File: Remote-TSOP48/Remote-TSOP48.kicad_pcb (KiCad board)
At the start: 2 copper layers, 32 x 23 mm, 12 parts, among them J1 FFC-50, J6 SHIELD, U1 TSOP-48

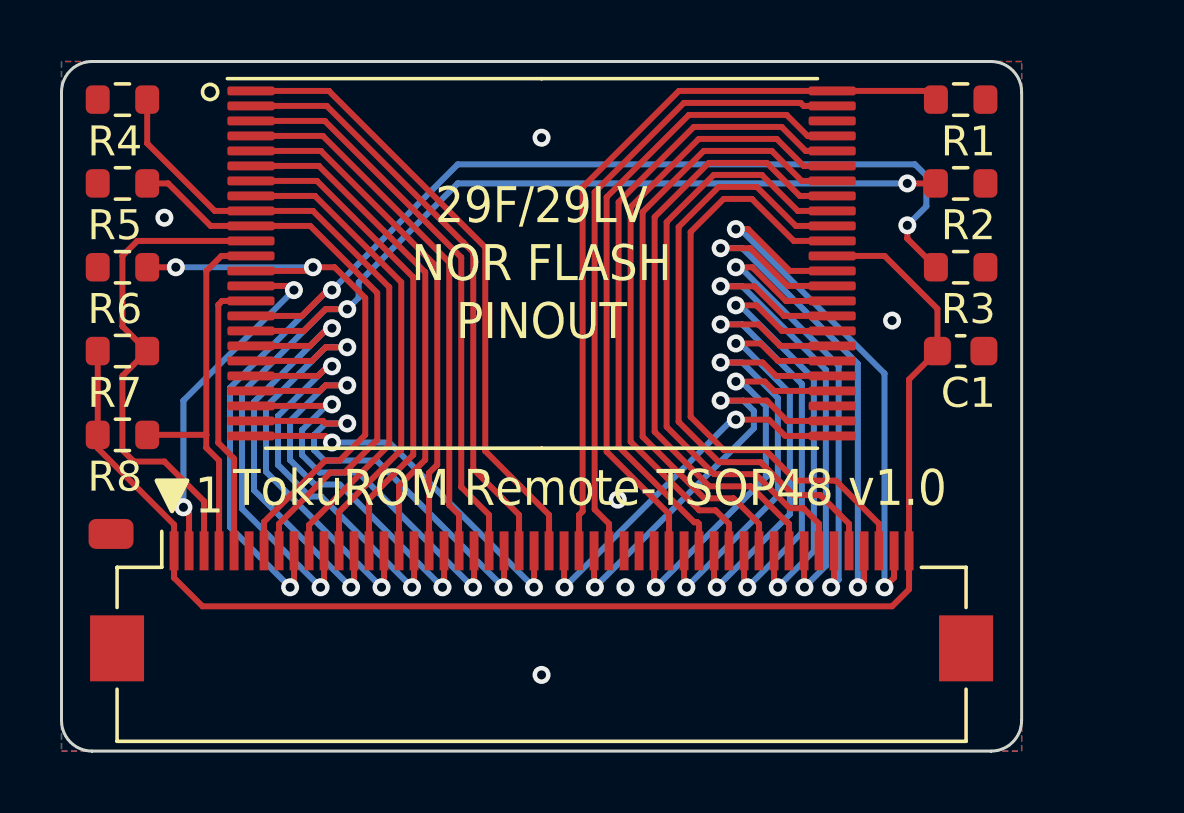
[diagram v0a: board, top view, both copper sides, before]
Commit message: Remote-TSOP48 v1.1 accomodates 0603 or 0805 passives, connector moved down
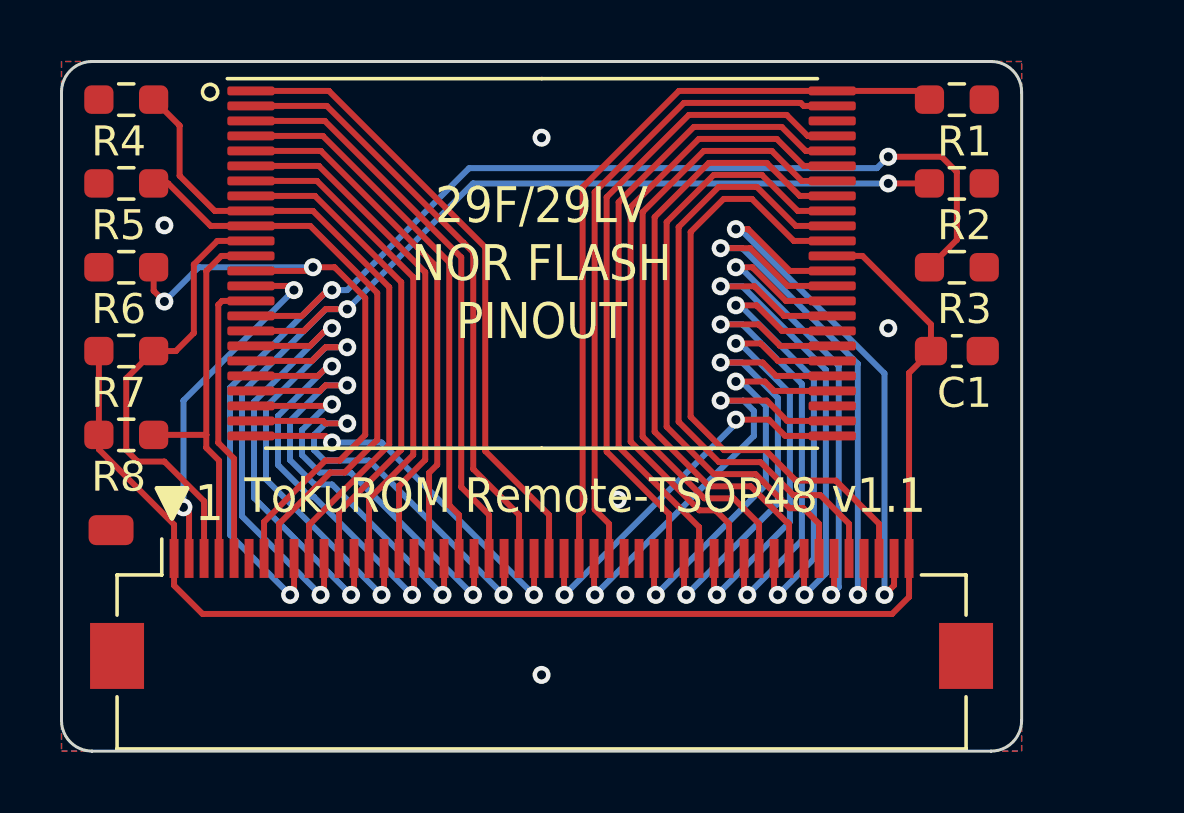
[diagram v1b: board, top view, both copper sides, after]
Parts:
- C1: footprint Capacitor_SMD:C_0603_1608Metric -> Capacitor_SMD:C_0603_1608Metric_Pad1.08x0.95mm_HandSolder
- R1, R2, R3, R4, R5, R6, R7, R8: footprint Resistor_SMD:R_0603_1608Metric -> Resistor_SMD:R_0603_1608Metric_Pad0.98x0.95mm_HandSolder
- moved J1 0.25 mm to (29.8, 32.4)
- moved J6 0.13 mm to (15.5, 29.6)
- moved R4 0.13 mm to (16.0, 15.2)
- moved R5 0.13 mm to (16.0, 18.0)
- moved R6 0.13 mm to (16.0, 20.8)
- moved R7 0.13 mm to (16.0, 23.6)
- moved R8 0.13 mm to (16.0, 26.4)
- moved C1 0.13 mm to (43.7, 23.6)
- moved R1 0.13 mm to (43.7, 15.2)
- moved R2 0.13 mm to (43.7, 18.0)
- moved R3 0.13 mm to (43.7, 20.8)
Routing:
- net /_WE: track 16.7 -> 15.0 mm
- net /A21: track 19.9 -> 21.4 mm
- net /A18: track 42.0 -> 43.2 mm
